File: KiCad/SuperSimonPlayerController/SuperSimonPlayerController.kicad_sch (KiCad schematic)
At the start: 1 part, among them U1 ESP32-S3-MINI-1-N8

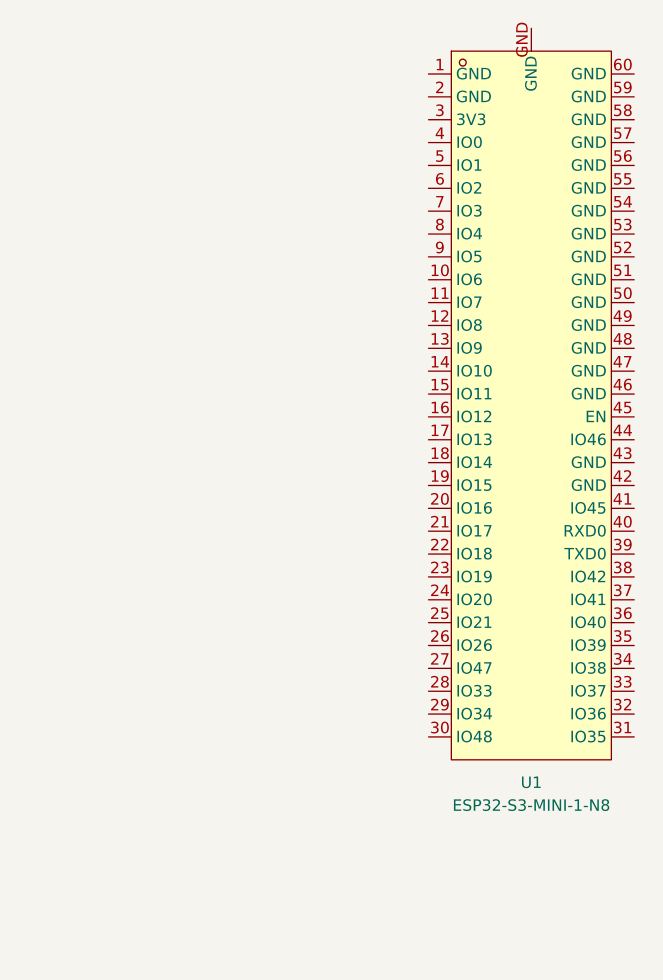
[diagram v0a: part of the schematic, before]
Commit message: Swapped to esp32-c3 with castallated pads, added some passives, created schematic sheet for the esp32
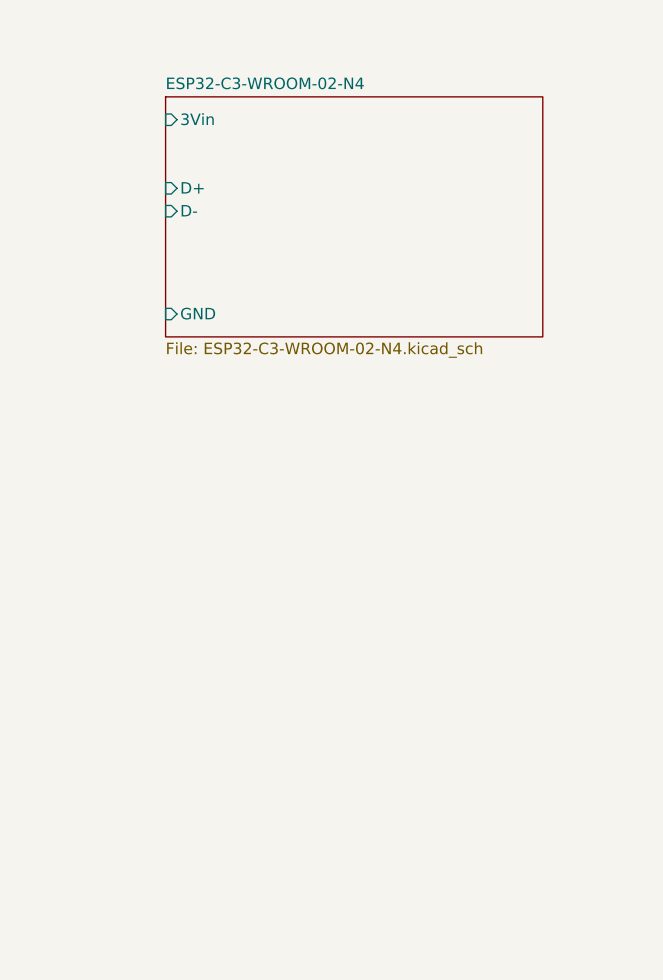
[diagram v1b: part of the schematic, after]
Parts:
- removed U1: ESP32-S3-MINI-1-N8, easyeda2kicad:BULETM-SMD_ESP32-S3-MINI-1-N8, symbol easyeda2kicad:ESP32-S3-MINI-1-N8
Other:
- added sheet ESP32-C3-WROOM-02-N4 (ESP32-C3-WROOM-02-N4.kicad_sch)
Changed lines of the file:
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@@
-		)
-	)
-	(symbol
-		(lib_id "easyeda2kicad:ESP32-S3-MINI-1-N8")
-		(at 189.23 73.66 0)
-		(unit 1)
-		(exclude_from_sim no)
-		(in_bom yes)
-		(on_board yes)
-		(dnp no)
-		(fields_autoplaced yes)
-		(property "Reference" "U1"
-			(at 189.23 115.57 0)
-			(effects
-				(font
-					(size 1.27 1.27)
-				)
-			)
-		)
-		(property "Value" "ESP32-S3-MINI-1-N8"
-			(at 189.23 118.11 0)
-			(effects
-				(font
-					(size 1.27 1.27)
-				)
-			)
-		)
-		(property "Footprint" "easyeda2kicad:BULETM-SMD_ESP32-S3-MINI-1-N8"
-			(at 189.23 118.11 0)
-			(effects
-				(font
-					(size 1.27 1.27)
-				)
-				(hide yes)
-			)
-		)
-		(property "Datasheet" ""
-			(at 189.23 73.66 0)
-			(effects
-				(font
-					(size 1.27 1.27)
-				)
-				(hide yes)
-			)
-		)
-		(property "Description" ""
-			(at 189.23 73.66 0)
-			(effects
-				(font
-					(size 1.27 1.27)
-				)
-				(hide yes)
-			)
-		)
-		(property "LCSC Part" "C2913206"
-			(at 189.23 120.65 0)
-			(effects
-				(font
-					(size 1.27 1.27)
-				)
-				(hide yes)
-			)
-		)
-		(pin "19"
-		)
-		(pin "49"
-		)
-		(pin "12"
-		)
-		(pin "18"
-		)
-		(pin "21"
-		)
-		(pin "26"
-		)
-		(pin "1"
-		)
-		(pin "2"
-		)
-		(pin "23"
-		)
-		(pin "24"
-		)
-		(pin "36"
-		)
-		(pin "37"
-		)
-		(pin "38"
-		)
-		(pin "39"
-		)
-		(pin "4"
-		)
-		(pin "29"
-		)
-		(pin "32"
-		)
-		(pin "17"
-		)
-		(pin "31"
-		)
-		(pin "11"
-		)
-		(pin "20"
-		)
-		(pin "22"
-		)
-		(pin "27"
-		)
-		(pin "10"
-		)
-		(pin "16"
-		)
-		(pin "28"
-		)
-		(pin "3"
-		)
-		(pin "14"
-		)
-		(pin "13"
-		)
-		(pin "33"
-		)
-		(pin "15"
-		)
-		(pin "25"
-		)
-		(pin "34"
-		)
-		(pin "30"
-		)
-		(pin "35"
-		)
-		(pin "60"
-		)
-		(pin "5"
-		)
-		(pin "9"
-		)
-		(pin "45"
-		)
-		(pin "48"
-		)
-		(pin "59"
-		)
-		(pin "42"
-		)
-		(pin "56"
-		)
-		(pin "57"
-		)
-		(pin "44"
-		)
-		(pin "7"
-		)
-		(pin "8"
-		)
-		(pin "50"
-		)
-		(pin "51"
-		)
-		(pin "53"
-		)
-		(pin "52"
-		)
-		(pin "55"
-		)
-		(pin "6"
-		)
-		(pin "41"
-		)
-		(pin "54"
-		)
-		(pin "43"
-		)
-		(pin "46"
-		)
-		(pin "40"
-		)
-		(pin "47"
-		)
-		(pin "58"
-		)
-		(pin "GND"
-		)
-		(instances
-			(project ""
-				(path "/16d29a44-aad0-40a4-ad73-624e48982eb8"
-					(reference "U1")
-					(unit 1)
-				)
-			)
 		)
 	)
@@
 				)
 			)
+		)
+	)
+	(sheet
+		(at 148.59 39.37)
+		(size 41.91 26.67)
+		(fields_autoplaced yes)
+		(stroke
+			(width 0.1524)
+			(type solid)
+		)
+		(fill
+			(color 255 229 191 1.0000)
+		)
+		(property "Sheetname" "ESP32-C3-WROOM-02-N4"
+			(at 148.59 38.6584 0)
+			(effects
+				(font
+					(size 1.27 1.27)
+				)
+				(justify left bottom)
+			)
+		)
+		(property "Sheetfile" "ESP32-C3-WROOM-02-N4.kicad_sch"
+			(at 148.59 66.6246 0)
+			(effects
+				(font
+					(size 1.27 1.27)
+				)
+				(justify left top)
+			)
+		)
+		(pin "GND" input
+			(at 148.59 63.5 180)
+			(effects
+				(font
+					(size 1.27 1.27)
+				)
+				(justify left)
+			)
+		)
+		(pin "3Vin" input
+			(at 148.59 41.91 180)
+			(effects
+				(font
+					(size 1.27 1.27)
+				)
+				(justify left)
+			)
+		)
+		(pin "D+" input
+			(at 148.59 49.53 180)
+			(effects
+				(font
+					(size 1.27 1.27)
+				)
+				(justify left)
+			)
+		)
+		(pin "D-" input
+			(at 148.59 52.07 180)
+			(effects
+				(font
+					(size 1.27 1.27)
+				)
+				(justify left)
+			)
+		)
+		(instances
+			(project "SuperSimonPlayerController"
+				(path "/16d29a44-aad0-40a4-ad73-624e48982eb8"
+					(page "3")
+				)
+			)
